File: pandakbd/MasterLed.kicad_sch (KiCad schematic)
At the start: 32 parts

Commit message: rev2
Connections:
- net at LED24.2 (DOUT): now also LED23.4 (DIN); no longer LED25.4 (DIN)
- net at LED23.2 (DOUT): now also LED22.4 (DIN); no longer LED24.4 (DIN)
- net at LED21.2 (DOUT): now also LED20.4 (DIN); no longer LED22.4 (DIN)
- net at LED21.4 (DIN): now also LED22.2 (DOUT); no longer LED20.2 (DOUT)
- net at LED10.4 (DIN): now also LED11.2 (DOUT); no longer LED9.2 (DOUT)
- net at LED9.4 (DIN): now also LED10.2 (DOUT); no longer LED8.2 (DOUT)
- net at LED32.2 (DOUT): now also LED31.4 (DIN)
- net at LED32.4 (DIN): now also LED30.2 (DOUT); no longer LED31.2 (DOUT)
- net at LED12.4 (DIN): now also LED6.2 (DOUT); no longer LED11.2 (DOUT)
- net at LED11.4 (DIN): now also LED12.2 (DOUT); no longer LED10.2 (DOUT)
- net at LED7.2 (DOUT): now also LED13.4 (DIN); no longer LED8.4 (DIN)
- net at LED7.4 (DIN): now also LED8.2 (DOUT); no longer LED6.2 (DOUT)
- net at LED19.2 (DOUT): now also LED25.4 (DIN); no longer LED20.4 (DIN)
- net at LED19.4 (DIN): now also LED20.2 (DOUT); no longer LED18.2 (DOUT)
- new net: LED8.4 (DIN), LED9.2 (DOUT)
- new net: LED18.2 (DOUT), LED24.4 (DIN)

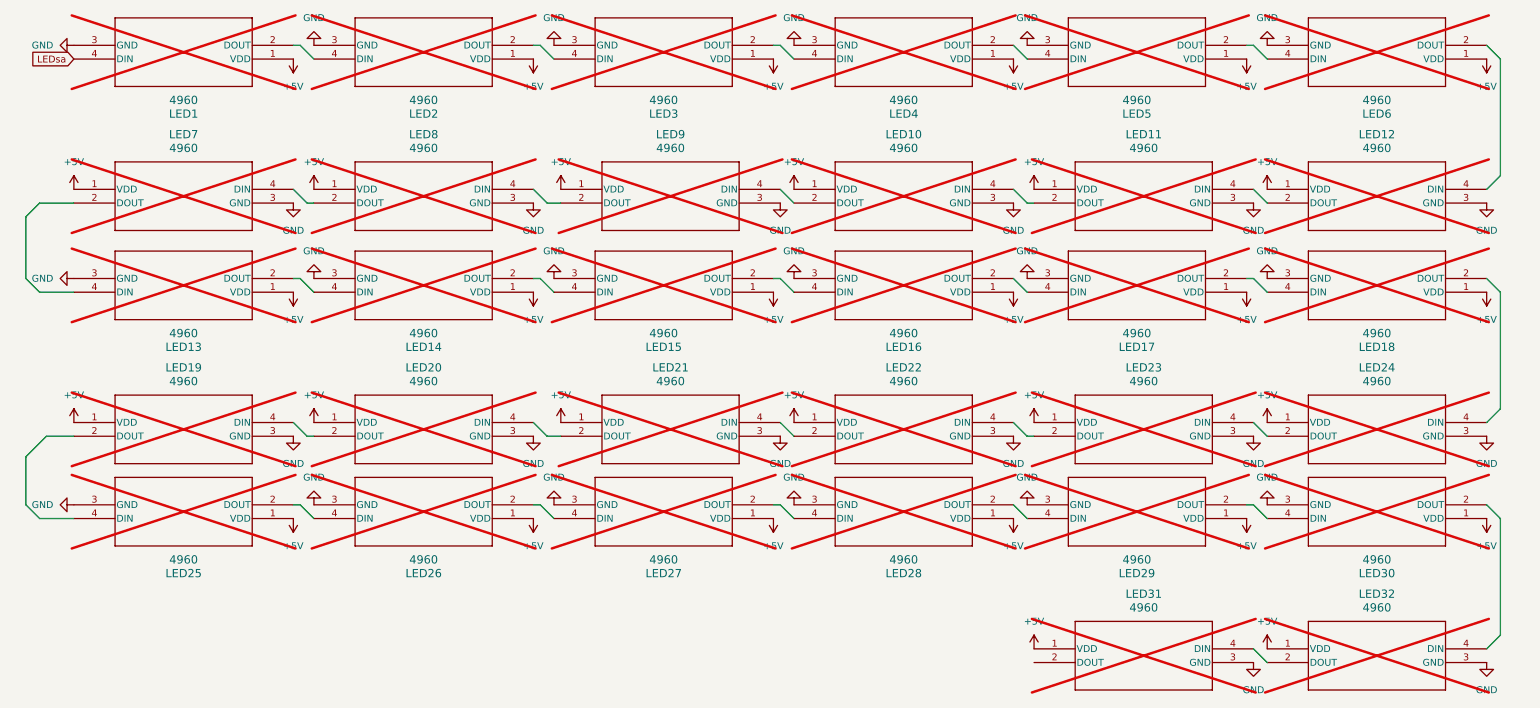
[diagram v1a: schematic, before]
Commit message: prepare placing components
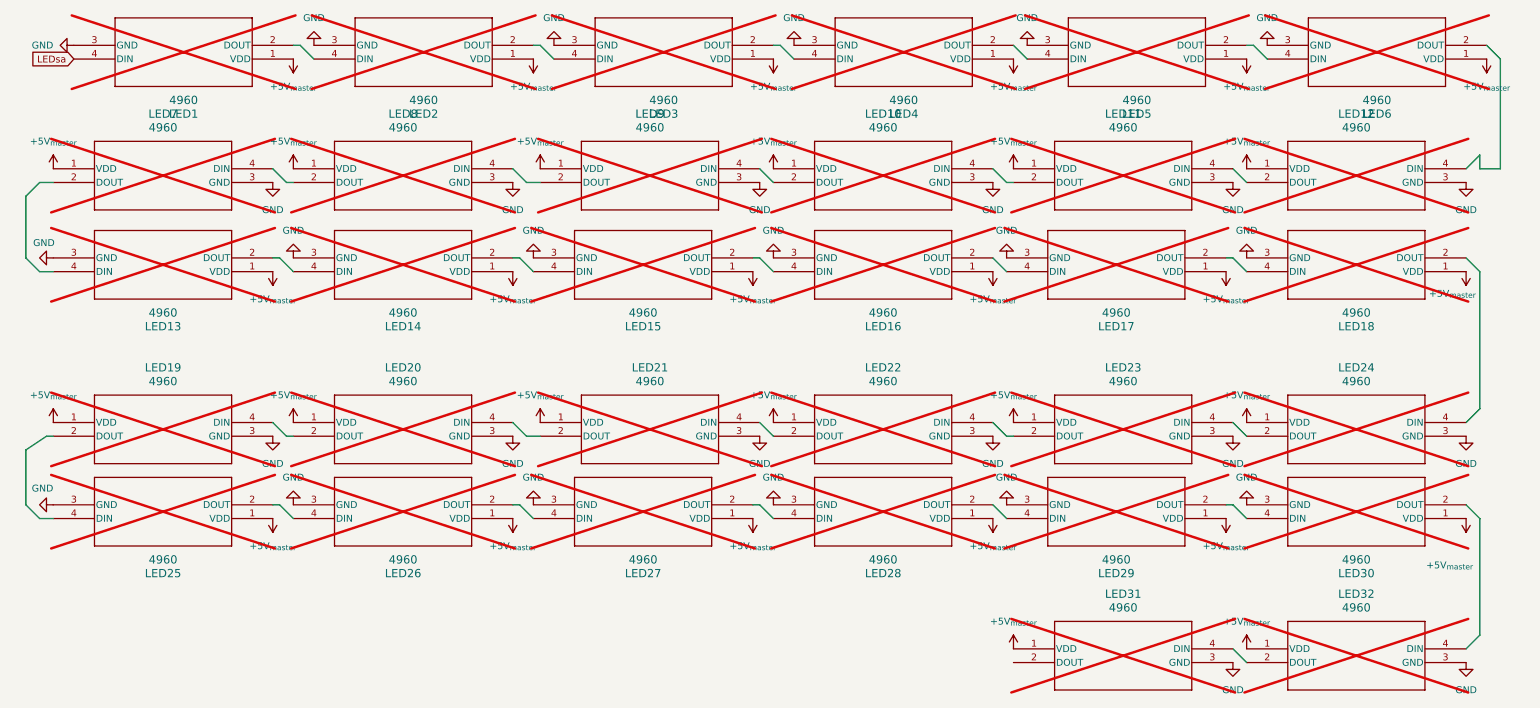
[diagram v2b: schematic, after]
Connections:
- net +5V renamed +5V_{master}
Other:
- moved on the sheet: LED10, LED11, LED12, LED13, LED14, LED15, LED16, LED17, LED18, LED19, LED20, LED21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
